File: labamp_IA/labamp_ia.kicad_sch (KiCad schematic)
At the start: 13 parts, among them J1 Conn_02x06_Odd_Even, J2 Conn_02x06_Odd_Even, J3 Conn_01x03

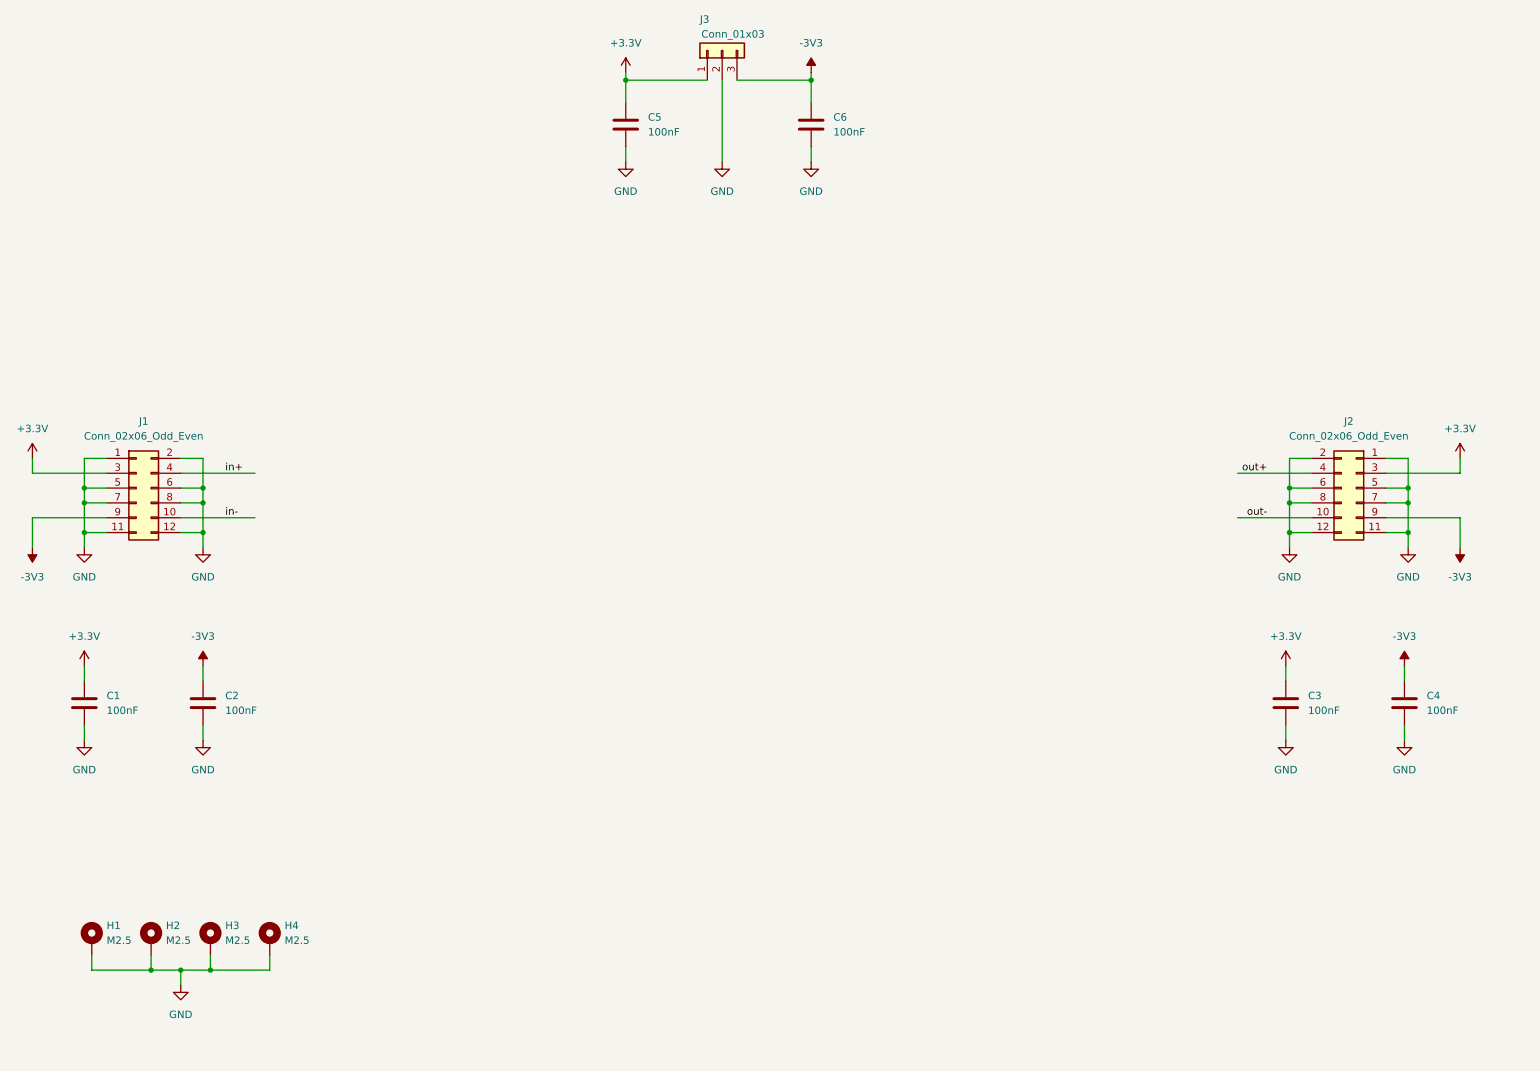
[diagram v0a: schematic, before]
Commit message: Added instrument amplificer schematics
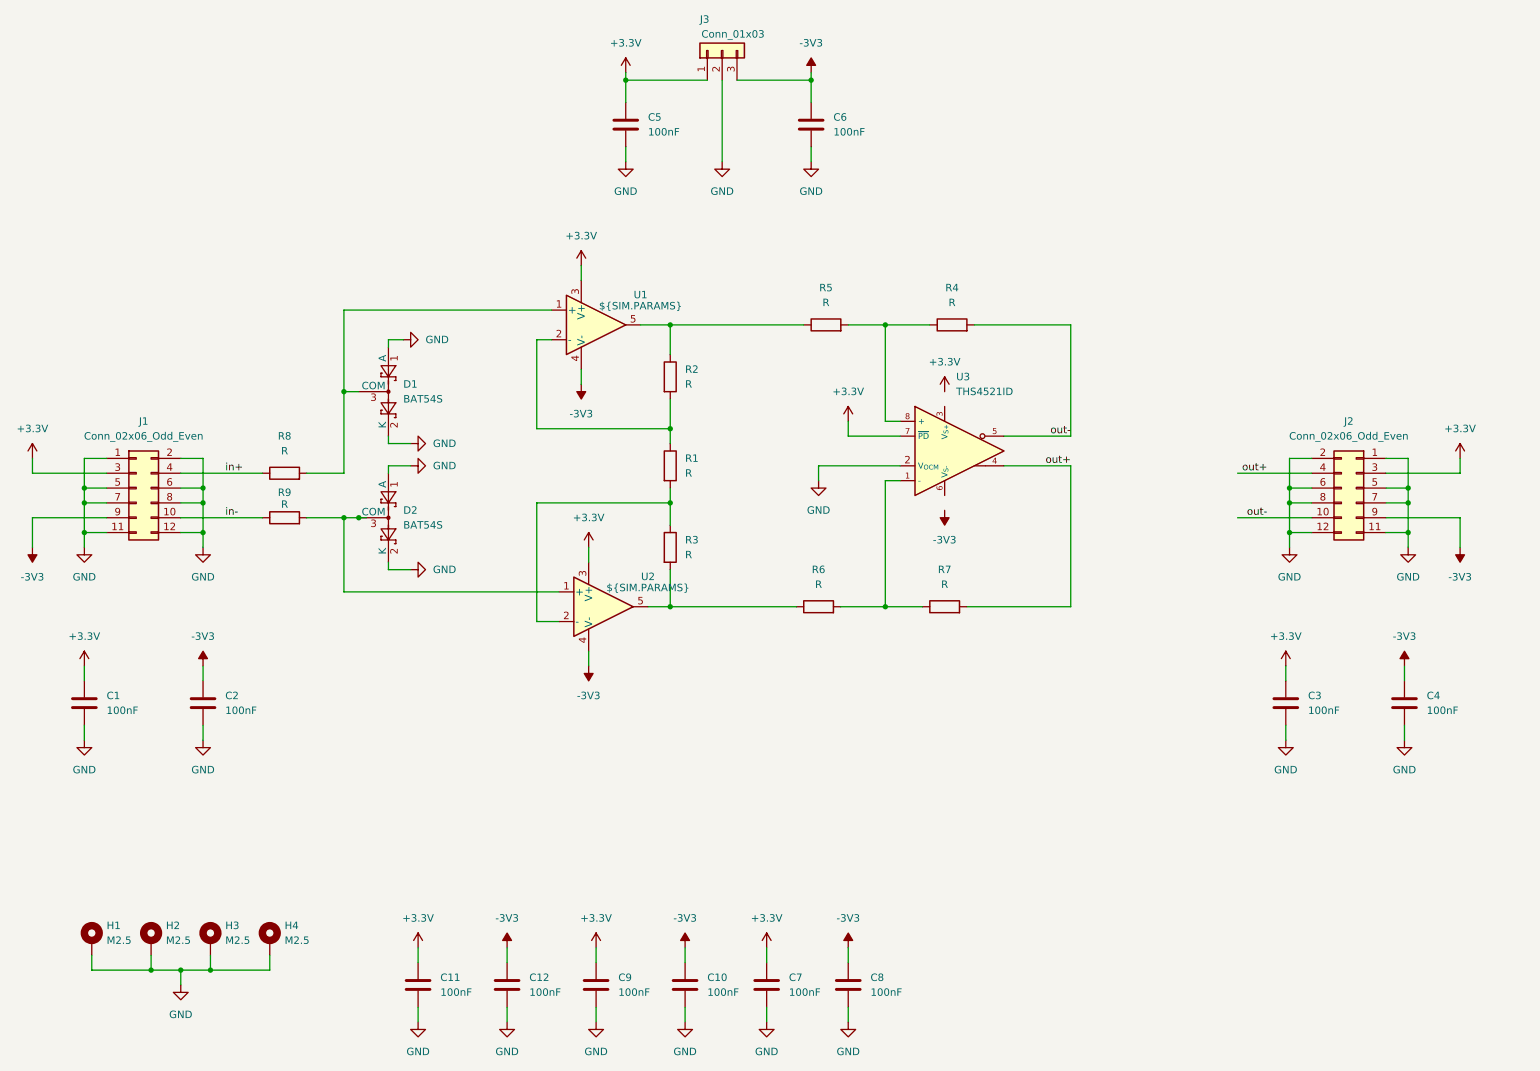
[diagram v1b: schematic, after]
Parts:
- added C10, C11, C12, C7, C8, C9: 100nF, Capacitor_SMD:C_0603_1608Metric_Pad1.08x0.95mm_HandSolder, symbol Device:C
- added D1, D2: BAT54S, Package_TO_SOT_SMD:SOT-23, symbol Diode:BAT54S
- added R1, R2, R3, R4, R5, R6, R7, R8, R9: R, Resistor_SMD:R_0603_1608Metric_Pad0.98x0.95mm_HandSolder, symbol Device:R
- added U1, U2: ${SIM.PARAMS}, SOT-23-5, symbol Simulation_SPICE:OPAMP
- added U3: THS4521ID, Package_SO:SOIC-8_3.9x4.9mm_P1.27mm, symbol Amplifier_Difference:THS4521ID
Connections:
- net +3.3V: now also C11.1, C7.1, C9.1, U1.3 (V+), U2.3 (V+), U3.7 (~{PD})
- net -3V3: now also C10.1, C12.1, C8.1, U1.4 (V-), U2.4 (V-)
- net GND: now also C10.2, C11.2, C12.2, C7.2, C8.2, C9.2, D1.1 (A), D1.2 (K), D2.1 (A), D2.2 (K), U3.2 (V_{OCM})
- net in+: now also R8.1
- net in-: now also R9.1
- net out+: now also R7.2, U3.4
- net out-: now also R4.2, U3.5
- new net: R6.2, R7.1, U3.1 (-)
- new net: R4.1, R5.2, U3.8 (+)
- new net: D2.3 (COM), R9.2, U2.1 (+)
- new net: R1.2, R3.1, U2.2 (-)
- new net: R3.2, R6.1, U2.5
- new net: R2.1, R5.1, U1.5
- new net: R1.1, R2.2, U1.2 (-)
- new net: D1.3 (COM), R8.2, U1.1 (+)

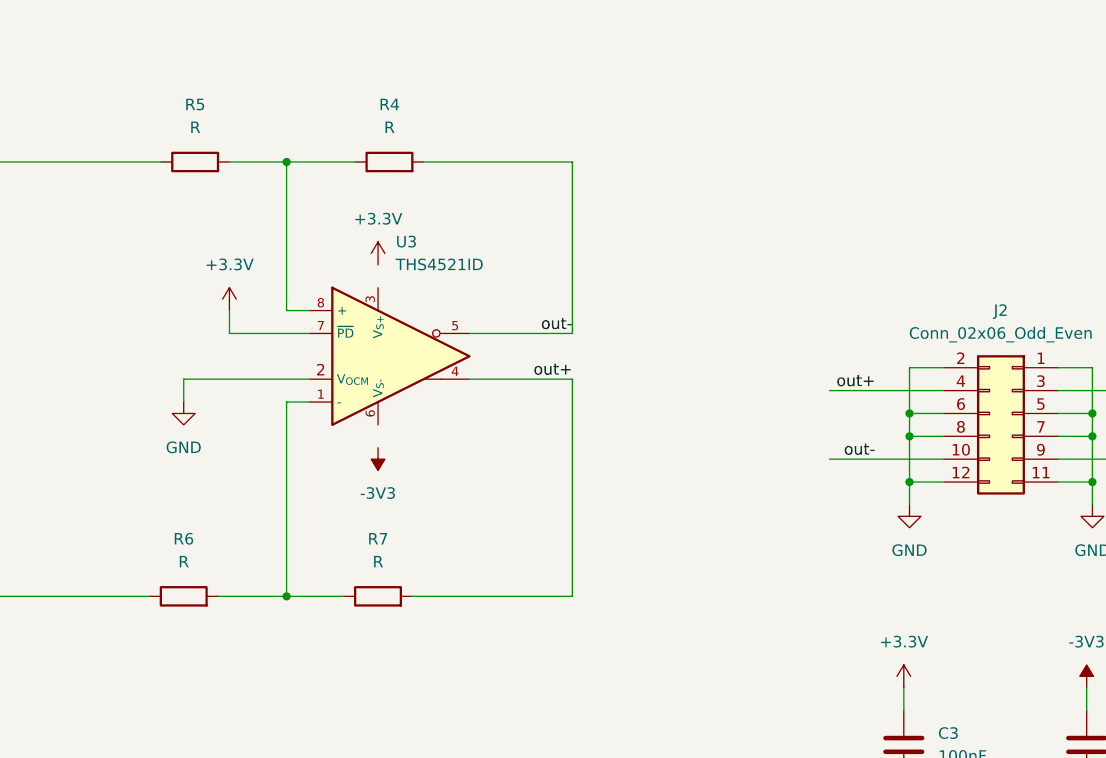
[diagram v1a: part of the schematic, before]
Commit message: Added output resistors to instrument amplifier schematics
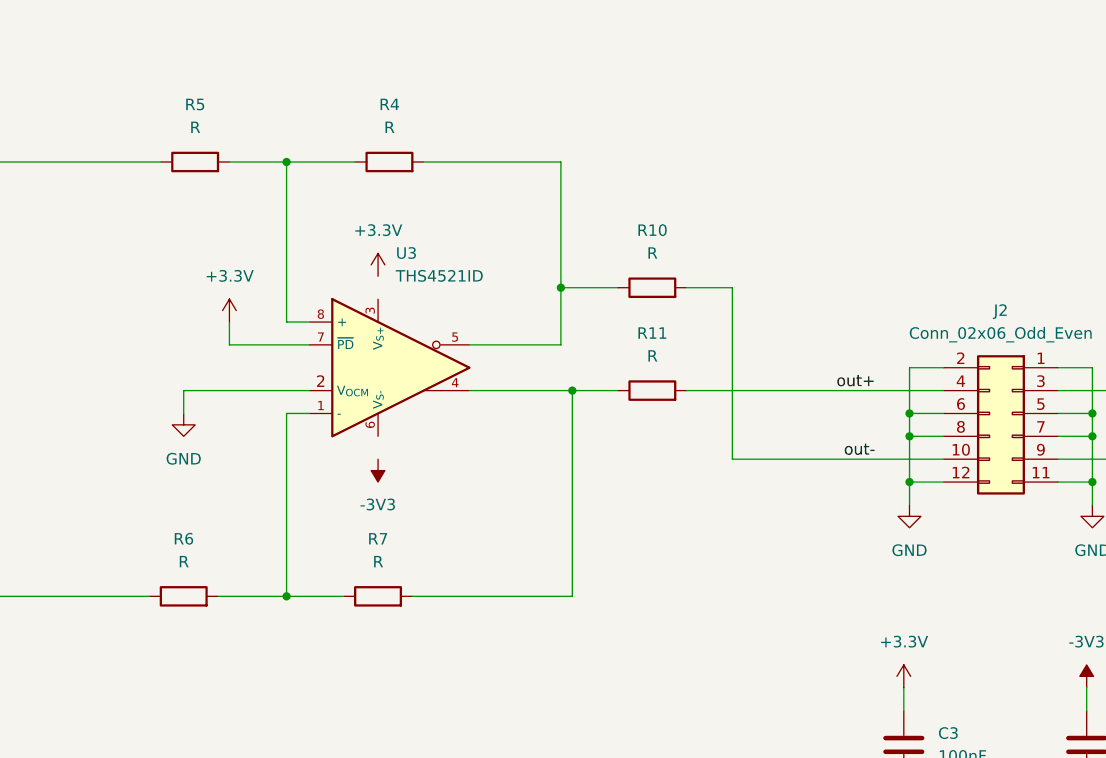
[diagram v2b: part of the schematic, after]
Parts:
- added R10, R11: R, Resistor_SMD:R_0603_1608Metric_Pad0.98x0.95mm_HandSolder, symbol Device:R
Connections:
- net out+: now also R11.2; no longer R7.2, U3.4
- net out-: now also R10.2; no longer R4.2, U3.5
- new net: R11.1, R7.2, U3.4
- new net: R10.1, R4.2, U3.5
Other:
- moved on the sheet: U3

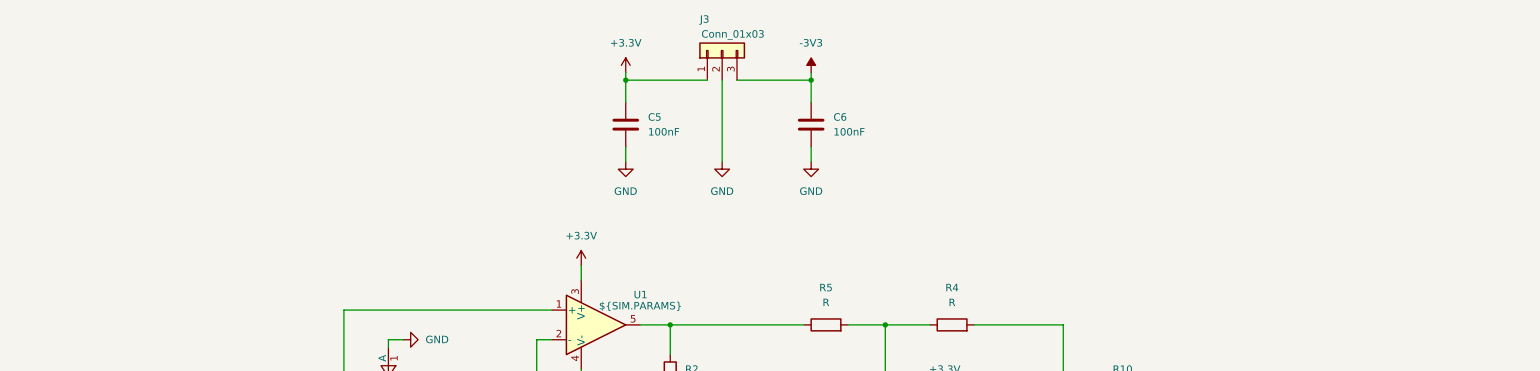
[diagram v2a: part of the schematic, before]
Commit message: Added notes and info to Instrument Amplifiser Schematics
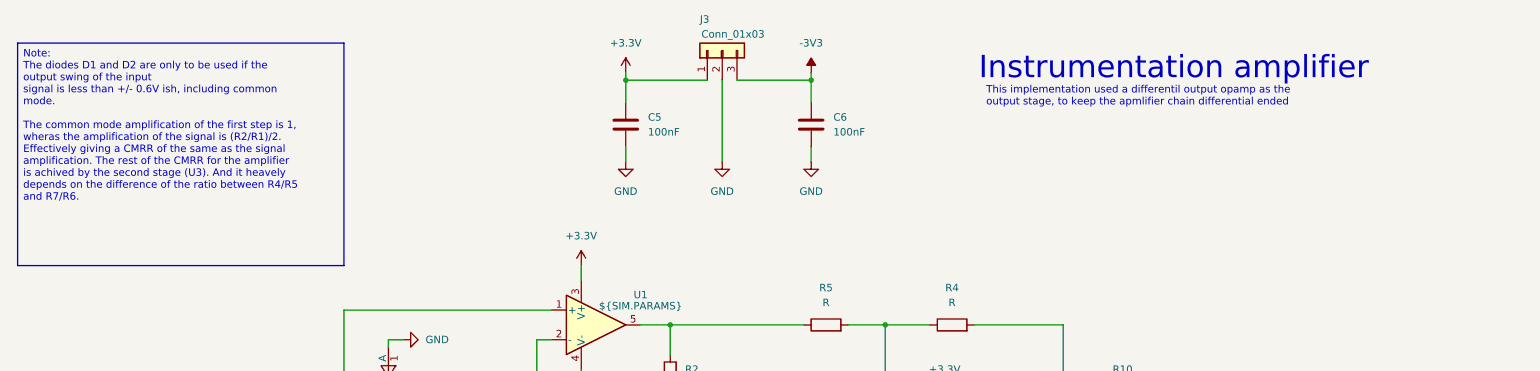
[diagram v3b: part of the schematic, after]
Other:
- note added: "Instrumentation amplifier"
- note added: "This implementation used a differentil output opamp as the output stage, to keep the apmlifier chain differential ended"
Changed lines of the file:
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@@
 	(generator_version "9.0")
 	(paper "A4")
+	(text "This implementation used a differentil output opamp as the \noutput stage, to keep the apmlifier chain differential ended"
+		(exclude_from_sim no)
+		(at 188.722 26.924 0)
+		(effects
+			(font
+				(size 1.27 1.27)
+			)
+			(justify left)
+		)
+	)
+	(text "Instrumentation amplifier\n"
+		(exclude_from_sim no)
+		(at 187.452 22.098 0)
+		(effects
+			(font
+				(size 3.81 3.81)
+			)
+			(justify left)
+		)
+	)
+	(text_box "Note:\nThe diodes D1 and D2 are only to be used if the output swing of the input\nsignal is less than +/- 0.6V ish, including common mode.\n\nThe common mode amplification of the first step is 1, wheras the amplification of the signal is (R2/R1)/2. \nEffectively giving a CMRR of the same as the signal amplification. The rest of the CMRR for the amplifier is achived by the second stage (U3). And it heavely depends on the difference of the ratio between R4/R5 and R7/R6.\n\n"
+		(exclude_from_sim no)
+		(at 22.86 17.78 0)
+		(size 55.88 38.1)
+		(margins 0.9525 0.9525 0.9525 0.9525)
+		(stroke
+			(width 0)
+			(type solid)
+		)
+		(fill
+			(type none)
+		)
+		(effects
+			(font
+				(size 1.27 1.27)
+			)
+			(justify left top)
+		)
+	)
 	(junction
 		(at 54.61 96.52)
